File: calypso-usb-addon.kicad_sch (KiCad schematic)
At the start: 11 parts, among them J1 Conn_02x12_Odd_Even, J2 Conn_02x12_Odd_Even, J3 USB_B_Micro, J4 USB_A_Stacked, J5 USB_A_Stacked, U1 HS8836A

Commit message: psram addition
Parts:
- added R3: 10K, Resistor_SMD:R_1206_3216Metric_Pad1.30x1.75mm_HandSolder, symbol Device:R
- added U2: ESP-PSRAM32, Package_SO:SOIC-8_3.9x4.9mm_P1.27mm, symbol Memory_RAM:ESP-PSRAM32
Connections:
- net +3.3VP: now also R3.1, U2.8 (VCC)
- net CYC_AUX0: now also R3.2, U2.1 (~{CE})
- net CYC_AUX1: now also U2.6 (SCLK)
- net CYC_AUX2: now also U2.7 (SIO3)
- net CYC_AUX3: now also U2.3 (SIO2)
- net CYC_AUX4: now also U2.5 (SI/SIO)
- net CYC_AUX5: now also U2.2 (SO/SIO)
- net GND: now also U2.4 (VSS)

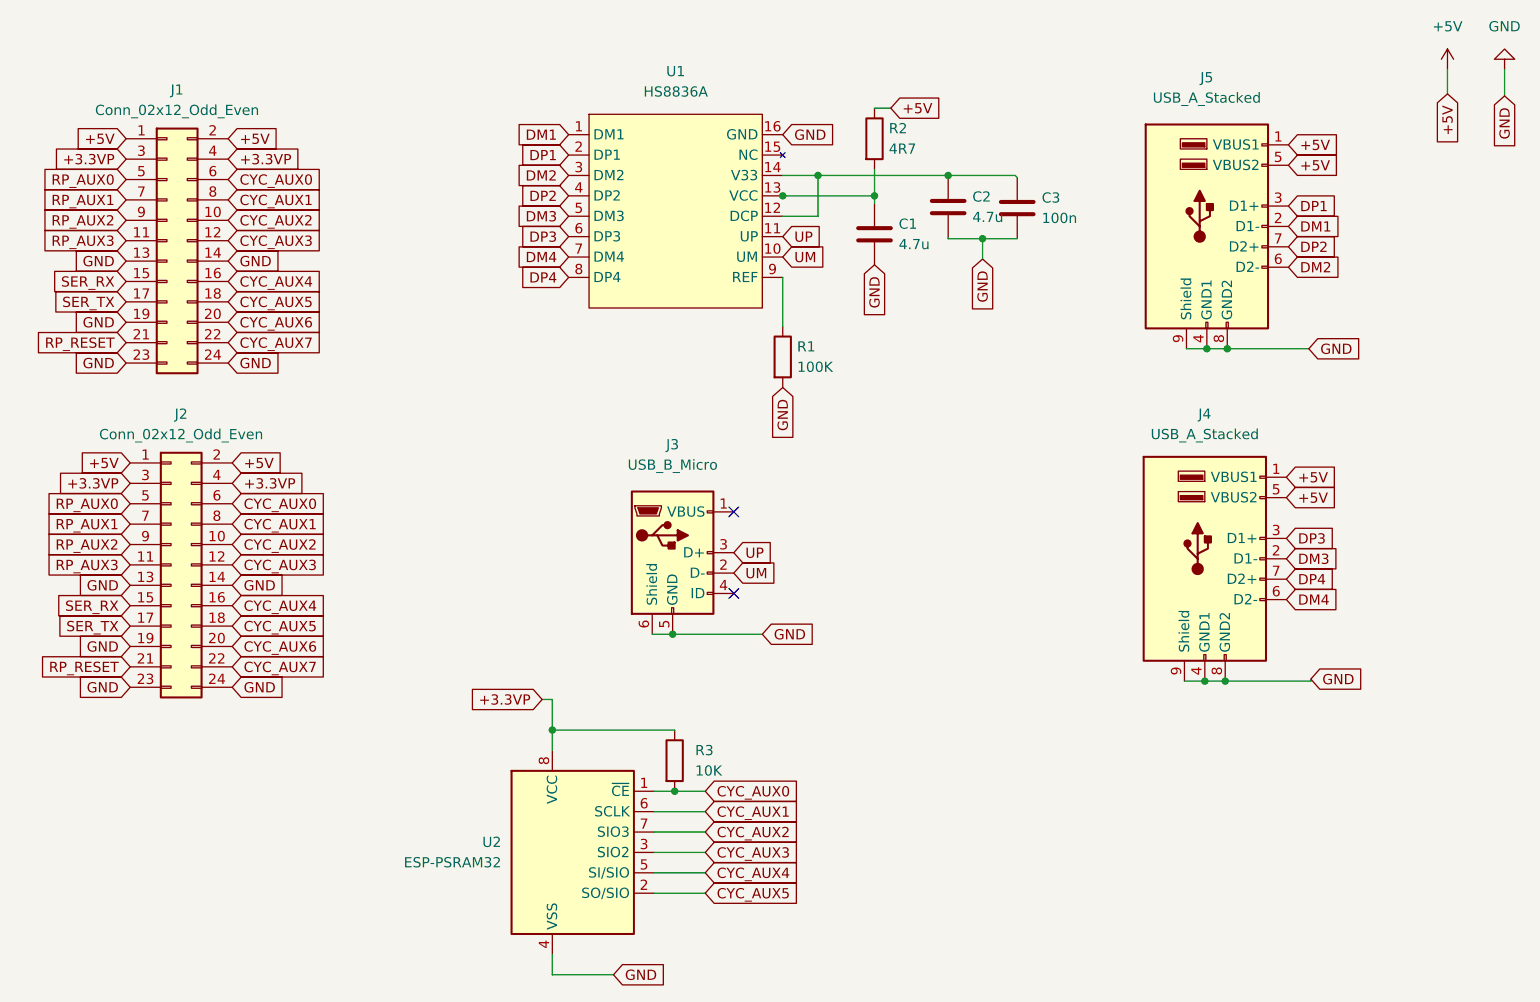
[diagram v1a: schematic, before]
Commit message: Fix connector lines
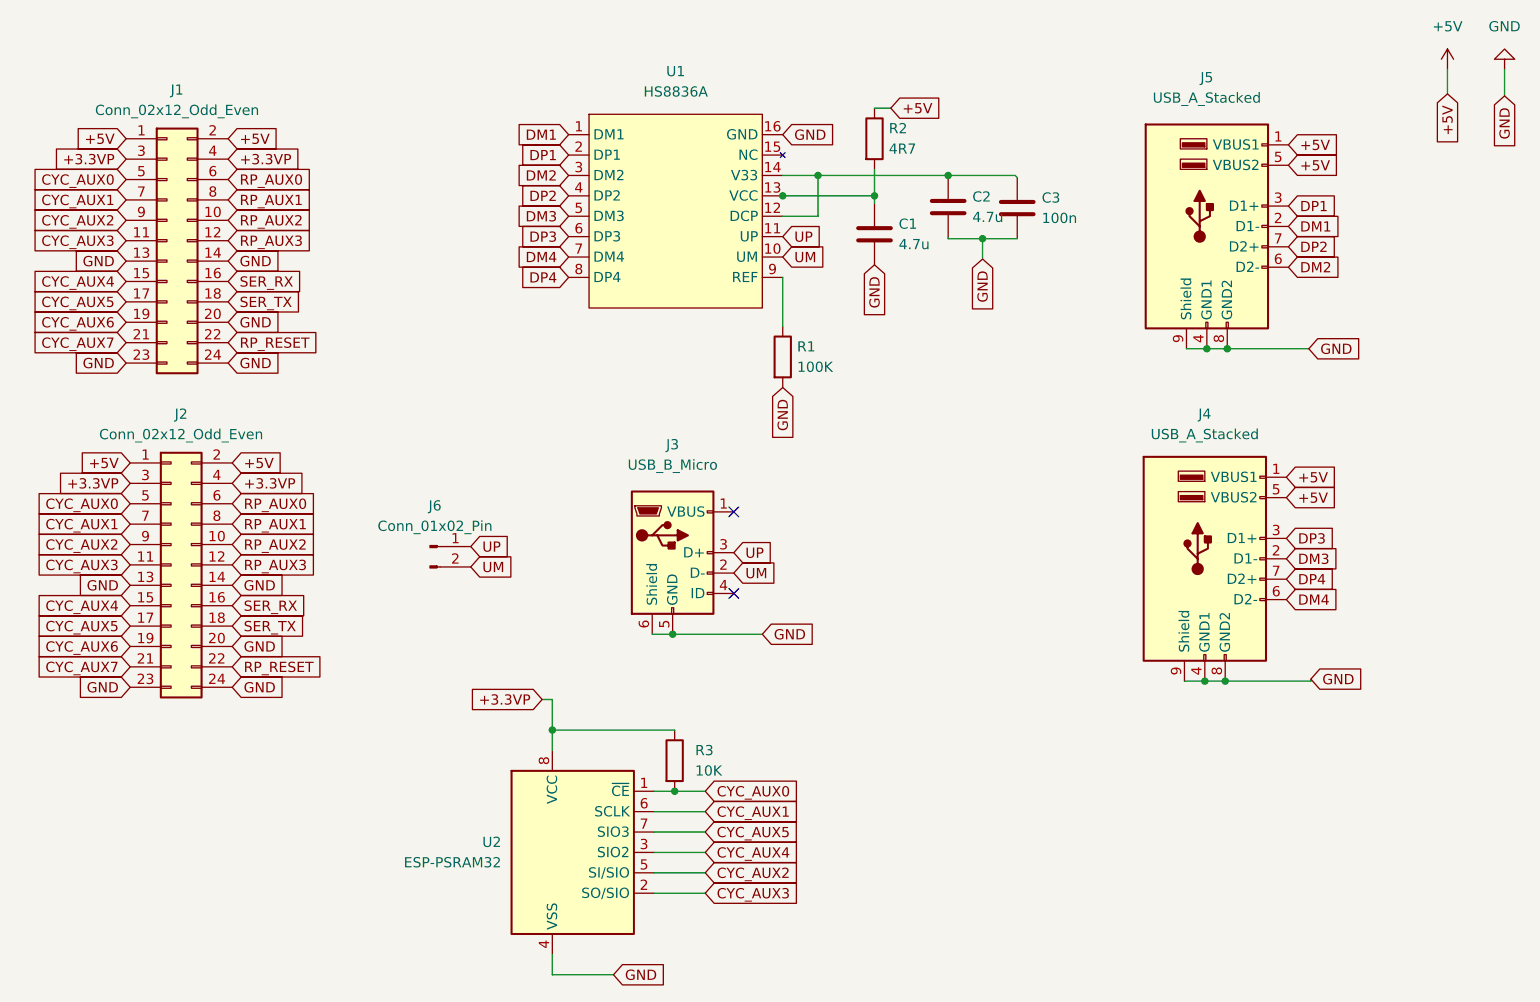
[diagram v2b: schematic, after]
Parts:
- added J6: Conn_01x02_Pin, Connector_PinHeader_2.54mm:PinHeader_1x02_P2.54mm_Vertical, symbol Connector:Conn_01x02_Pin
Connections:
- net CYC_AUX0: now also J1.5 (Pin_5), J2.5 (Pin_5); no longer J1.6 (Pin_6), J2.6 (Pin_6)
- net CYC_AUX1: now also J1.7 (Pin_7), J2.7 (Pin_7); no longer J1.8 (Pin_8), J2.8 (Pin_8)
- net CYC_AUX2: now also J1.9 (Pin_9), J2.9 (Pin_9), U2.5 (SI/SIO); no longer J1.10 (Pin_10), J2.10 (Pin_10), U2.7 (SIO3)
- net CYC_AUX3: now also J1.11 (Pin_11), J2.11 (Pin_11), U2.2 (SO/SIO); no longer J1.12 (Pin_12), J2.12 (Pin_12), U2.3 (SIO2)
- net CYC_AUX4: now also J1.15 (Pin_15), J2.15 (Pin_15), U2.3 (SIO2); no longer J1.16 (Pin_16), J2.16 (Pin_16), U2.5 (SI/SIO)
- net CYC_AUX5: now also J1.17 (Pin_17), J2.17 (Pin_17), U2.7 (SIO3); no longer J1.18 (Pin_18), J2.18 (Pin_18), U2.2 (SO/SIO)
- net CYC_AUX6: now also J1.19 (Pin_19), J2.19 (Pin_19); no longer J1.20 (Pin_20), J2.20 (Pin_20)
- net CYC_AUX7: now also J1.21 (Pin_21), J2.21 (Pin_21); no longer J1.22 (Pin_22), J2.22 (Pin_22)
- net GND: now also J1.20 (Pin_20), J2.20 (Pin_20); no longer J1.19 (Pin_19), J2.19 (Pin_19)
- net RP_AUX0: now also J1.6 (Pin_6), J2.6 (Pin_6); no longer J1.5 (Pin_5), J2.5 (Pin_5)
- net RP_AUX1: now also J1.8 (Pin_8), J2.8 (Pin_8); no longer J1.7 (Pin_7), J2.7 (Pin_7)
- net RP_AUX2: now also J1.10 (Pin_10), J2.10 (Pin_10); no longer J1.9 (Pin_9), J2.9 (Pin_9)
- net RP_AUX3: now also J1.12 (Pin_12), J2.12 (Pin_12); no longer J1.11 (Pin_11), J2.11 (Pin_11)
- net RP_RESET: now also J1.22 (Pin_22), J2.22 (Pin_22); no longer J1.21 (Pin_21), J2.21 (Pin_21)
- net SER_RX: now also J1.16 (Pin_16), J2.16 (Pin_16); no longer J1.15 (Pin_15), J2.15 (Pin_15)
- net SER_TX: now also J1.18 (Pin_18), J2.18 (Pin_18); no longer J1.17 (Pin_17), J2.17 (Pin_17)
- net UM: now also J6.2 (Pin_2)
- net UP: now also J6.1 (Pin_1)
